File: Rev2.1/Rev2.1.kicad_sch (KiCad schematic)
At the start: 32 parts, among them J1 Termination, J10 GPIO, J12 5V power breakout, J2 CAN1, J3 Termination, J4 CAN2, J5 3.3V power breakout, J6 LIN Pots, J7 AIN, U1 STM32F429ZITx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

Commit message: added pull up resistors to the I2c Lines for LSM and did mock up placements for PCB
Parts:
- removed J10: GPIO, TerminalBlock_Phoenix:TerminalBlock_Phoenix_MKDS-1,5-8_1x08_P5.00mm_Horizontal, symbol Connector:Screw_Terminal_01x08
- added J14: GPIO2, TerminalBlock_Phoenix:TerminalBlock_Phoenix_MKDS-1,5-4_1x04_P5.00mm_Horizontal, symbol Connector:Screw_Terminal_01x04
- added J7: GPIO1, TerminalBlock_Phoenix:TerminalBlock_Phoenix_MKDS-1,5-4_1x04_P5.00mm_Horizontal, symbol Connector:Screw_Terminal_01x04
- added R45, R46: 2k2, Resistor_SMD:R_0603_1608Metric_Pad0.98x0.95mm_HandSolder, symbol Device:R_Small
- renumbered R16 to R15, R15 to R16, R24 to R22, R22 to R24
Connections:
- net +3.3V: now also R45.1, R46.1
- net A1: now also R17.1, R9.2; no longer R12.2, R19.1
- net A2: now also R10.2, R18.1; no longer R11.2, R23.1
- net A3: now also R11.2, R23.1; no longer R10.2, R18.1
- net A4: now also R12.2, R19.1; no longer R17.1, R9.2
- net CAN1+: now also J2.2 (Pin_2); no longer J2.1 (Pin_1)
- net CAN1-: now also J2.1 (Pin_1); no longer J2.2 (Pin_2)
- net CAN2+: now also J4.2 (Pin_2); no longer J4.1 (Pin_1)
- net CAN2-: now also J4.1 (Pin_1); no longer J4.2 (Pin_2)
- net GPIO1: now also J7.1 (Pin_1)
- net GPIO2: now also J7.2 (Pin_2)
- net GPIO3: now also J7.3 (Pin_3)
- net GPIO4: now also J7.4 (Pin_4)
- net GPIO5: now also J14.1 (Pin_1)
- net GPIO6: now also U1.11 (PF1), J14.2 (Pin_2); no longer U1.7 (PC13)
- net GPIO7: now also J14.3 (Pin_3)
- net GPIO8: now also J14.4 (Pin_4)
- net LSM6DSOX_SCL: now also R45.2
- net LSM6DSOX_SDA: now also R46.2

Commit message: done about 2/3 of the routing for the board
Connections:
- net A1: now also R12.2, R19.1; no longer R17.1, R9.2
- net A2: now also R17.1, R9.2; no longer R10.2, R18.1
- net A4: now also R10.2, R18.1; no longer R12.2, R19.1
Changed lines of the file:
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@@
     )
   )
-  (global_label "A2" (shape input) (at 47.625 188.595 0) (fields_autoplaced)
+  (global_label "A4" (shape input) (at 47.625 188.595 0) (fields_autoplaced)
     (effects (font (size 1.27 1.27) (color 132 0 0 1)) (justify left))
     (property "Intersheetrefs" "${INTERSHEET_REFS}" (at 52.9083 188.595 0)
@@
     )
   )
-  (global_label "A4" (shape input) (at 61.595 188.595 0) (fields_autoplaced)
+  (global_label "A1" (shape input) (at 61.595 188.595 0) (fields_autoplaced)
     (effects (font (size 1.27 1.27) (color 132 0 0 1)) (justify left))
     (property "Intersheetrefs" "${INTERSHEET_REFS}" (at 66.8783 188.595 0)
@@
     )
   )
-  (global_label "A1" (shape input) (at 40.64 188.595 0) (fields_autoplaced)
+  (global_label "A2" (shape input) (at 40.64 188.595 0) (fields_autoplaced)
     (effects (font (size 1.27 1.27) (color 132 0 0 1)) (justify left))
     (property "Intersheetrefs" "${INTERSHEET_REFS}" (at 45.9233 188.595 0)

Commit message: finished the first mock up of routing now just need to polish it up
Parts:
- added H1, H2, H3, H4: MountingHole_Pad, MountingHole:MountingHole_3.2mm_M3_Pad_Via, symbol Mechanical:MountingHole_Pad
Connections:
- net GND: now also H1.1, H2.1, H3.1, H4.1
- net at U1.110 (PA15): no longer U2.8 (S)
- net at U1.77 (PD8): no longer U3.8 (S)
- net Silent_Mode1: now reaches U1.116 (PD2)
- net Silent_Mode1: now also U2.8 (S)
- net Silent_Mode2: now reaches U1.134 (PB4)
- net Silent_Mode2: now also U3.8 (S)

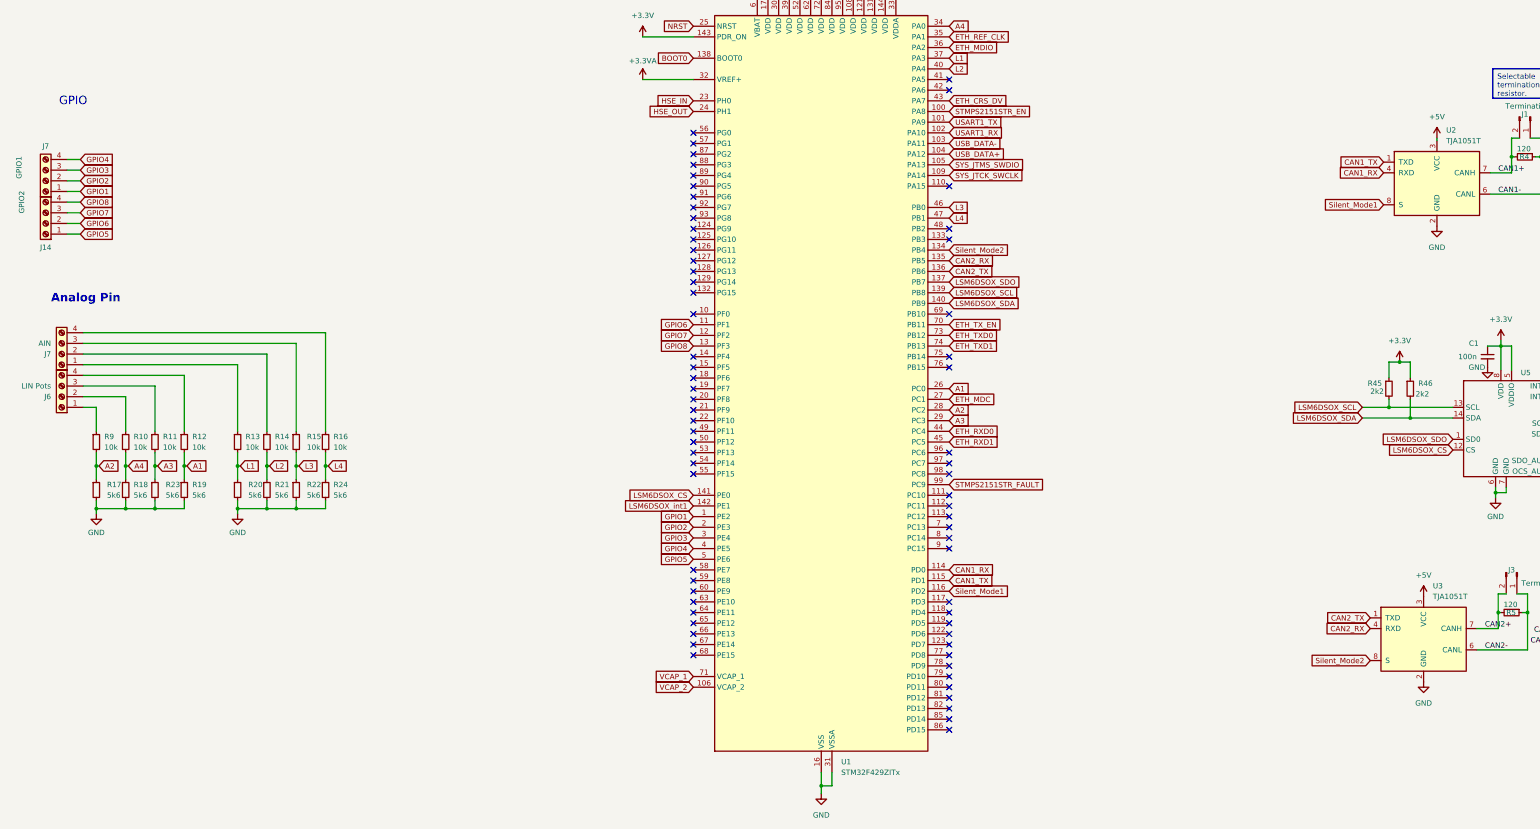
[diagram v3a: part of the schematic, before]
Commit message: added USART6 to some pin headers and added more labels and color codes to th schematic
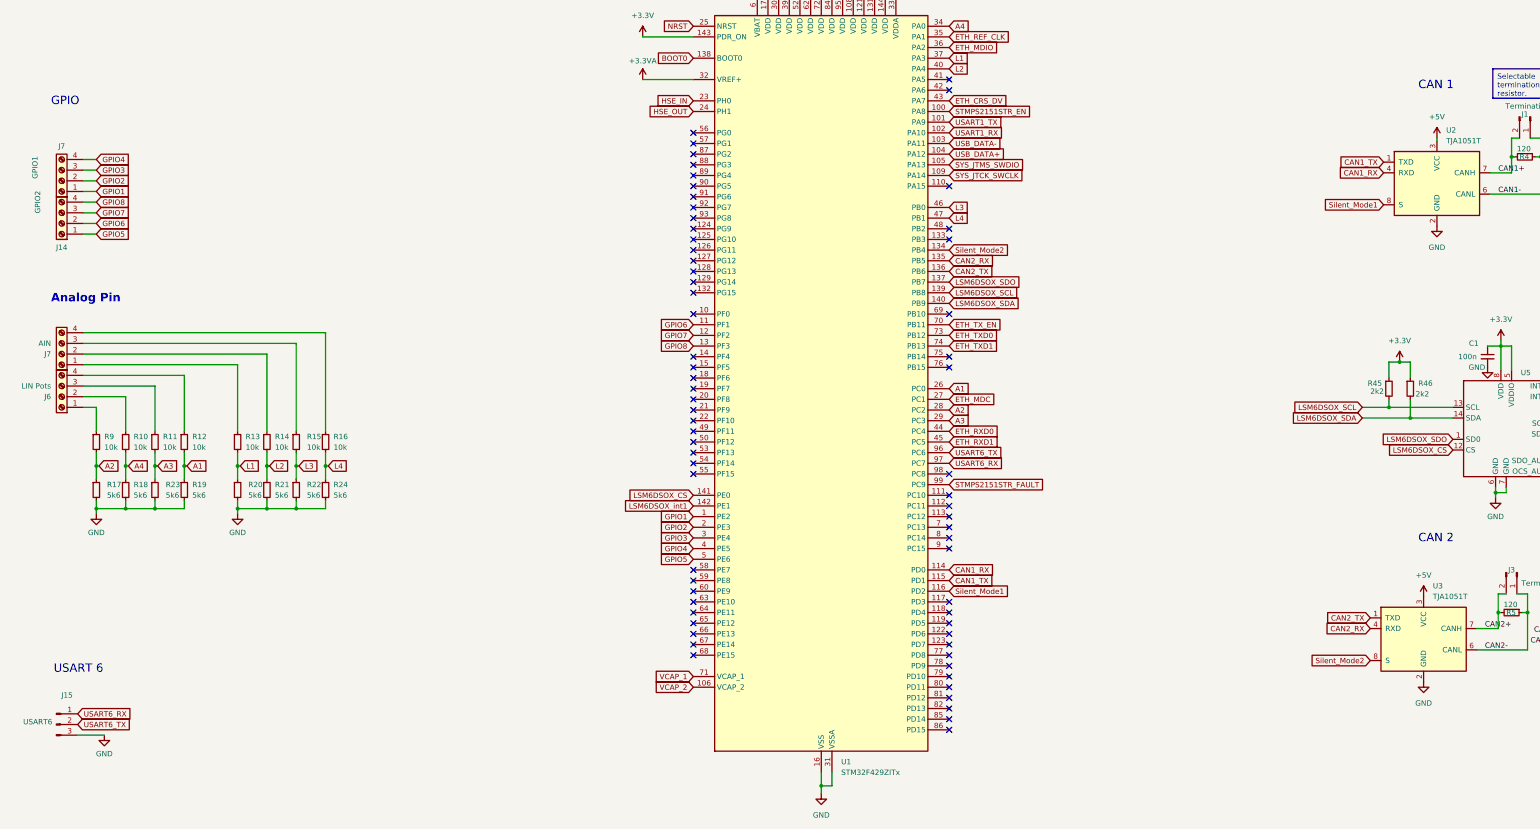
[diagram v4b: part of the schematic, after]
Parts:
- added J15: USART6, Connector_PinHeader_2.54mm:PinHeader_1x03_P2.54mm_Vertical, symbol Connector:Conn_01x03_Pin
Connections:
- net GND: now also J15.3 (Pin_3)
- net USART6_TX: now reaches U1.96 (PC6)
- net USART6_TX: now also J15.2 (Pin_2)
- net USART6_RX: now reaches U1.97 (PC7)
- net USART6_RX: now also J15.1 (Pin_1)
- no-connect marks 71 -> 69
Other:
- note added: "CAN 1"
- note added: "CAN 2"
- note added: "USART 6"
- moved on the sheet: J14, J7
